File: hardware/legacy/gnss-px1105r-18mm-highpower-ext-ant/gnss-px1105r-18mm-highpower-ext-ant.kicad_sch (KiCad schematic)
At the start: 32 parts, among them J4 BM05B-SRSS-TB, J9 2337019-1, U1 PX1105R, U3 TPS62913RPUR

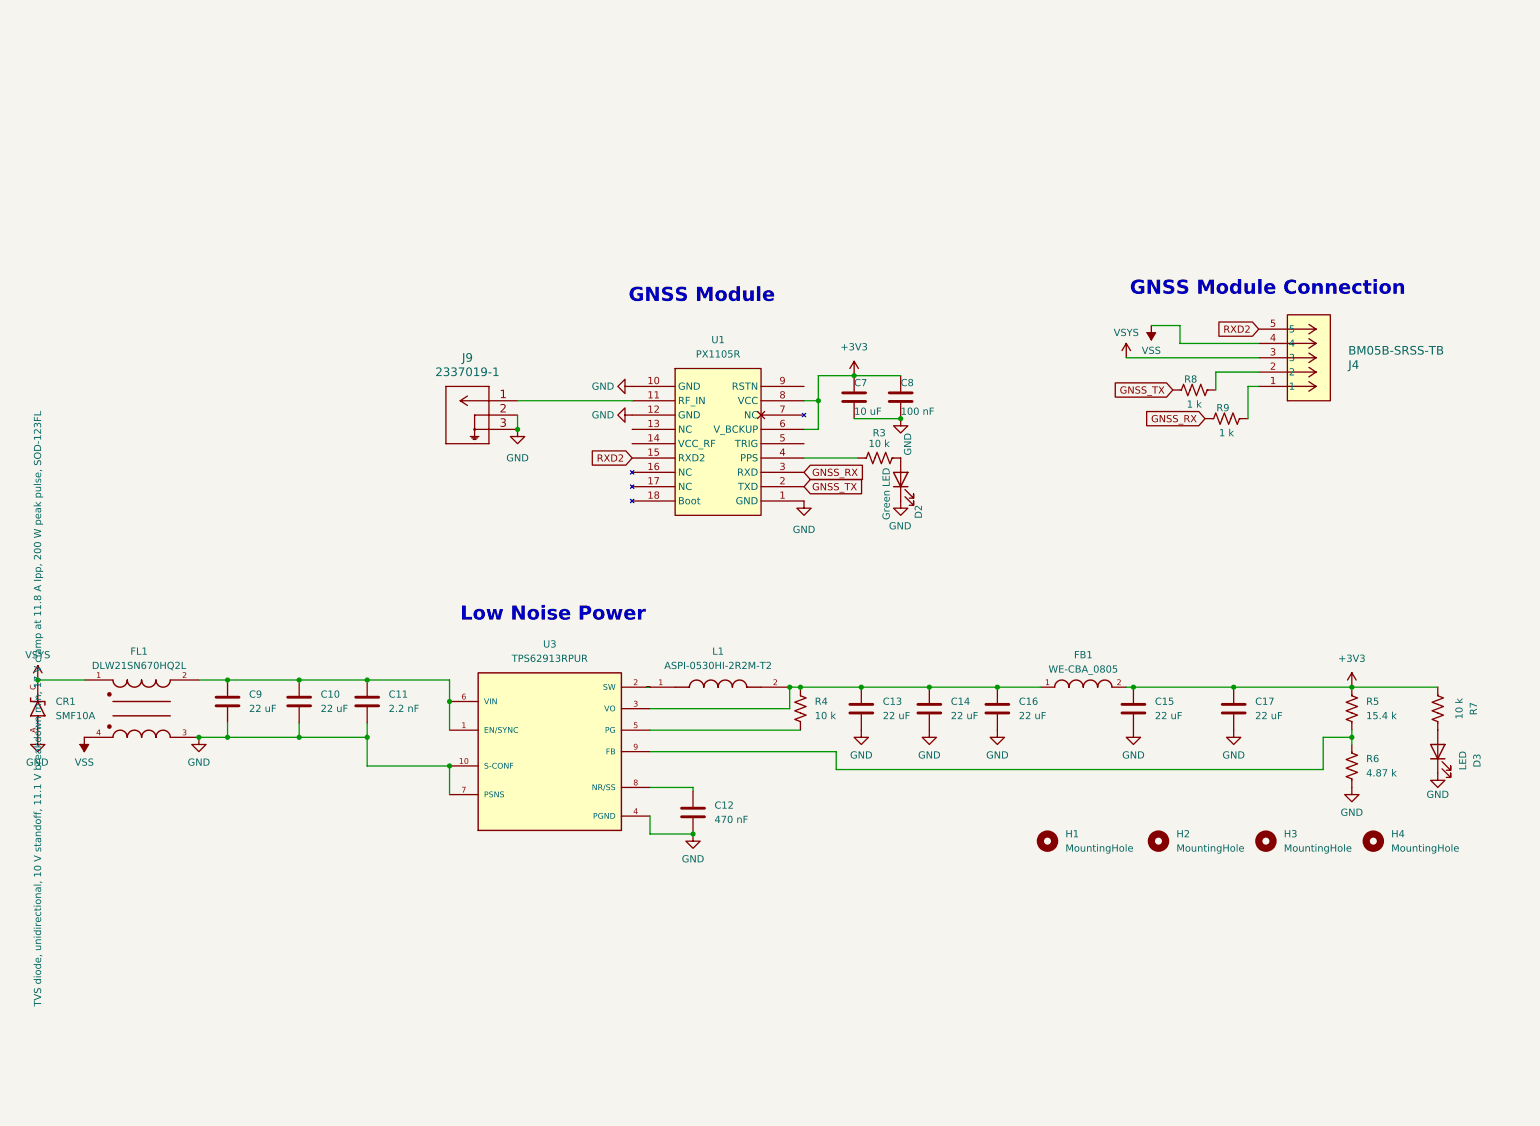
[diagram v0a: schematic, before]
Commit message: hardware(Space Bug): the PX1105R board redrawn as the Space Bug V2 -- ESP32-P4, IMU and a patch-antenna front end on 8 layers, its design review and fixes, and fab notes for the order (#1547)
hardware/legacy/gnss-px1105r-18mm-highpower-ext-ant now holds a new board:
35 x 35 mm, 8 layers on JLC08161H-2116. The PX1105R receiver sits on its own
LDO behind a filter-first dual-band front end (SAW, LNA, SAW, LNA) for a patch
antenna on the back, with an ESP32-P4 (chip revision v3.x) and 16 MB boot
flash, an ISM6HG256X IMU and USB-C. It keeps V2: the 4-layer V2 of 2026-08-15
was never fabricated (docs/board-versioning.md).

The design review (design-review-2026-09-27.md) now opens with a status table.
Fixed here, one finding at a time with the owner:
- Layout: L1 GNSS plane confined west of FL3; L2 feed keep-out on In3-In6;
  L3/L4 return vias; L6 test-pad traces; L7 vias in U2's exposed pad; L8 buck
  input and PGND; L9/L10 P4 supply widths and decoupling; L11 flash ground;
  L12 R11 at J4; L13 three fiducials; L15 different-net vias at 0.25 mm.
- Schematic: S2 J4's tabs to GND; S4 the receiver's BOOT_SEL on GPIO15
  through a DTC123J (Q1). D2 fills the four sheets' title blocks.
- Shared footprints: S8 PX1105R pasted at full pad; S9 QFN-16 keeps only its
  four panes; S10 TSNP single mask window and DPY +0.05 mm mask; S11 the
  SOIC-8-EP paste becomes four 1.0 mm panes. The SAM carrier's U2 shows a
  library mismatch until it is updated from the library.
- S7: cables.md says what a reversed 5-pin cable does to this board.
- D1/D7: FABRICATION-NOTES.md carries the block for the order: stackup,
  ENIG, Type VII vias (161 in lands), RF 0.18/0.20 mm = 50 ohm, mask webs,
  minimums, stencil, U1's 240 C reflow ceiling, placement and hand work.
- The board setup declares filled and capped vias, as the other multilayer
  boards do. Gerbers, drills and the job file are byte-identical either way.

Checks: DRC 0 errors, 0 unconnected (10 old silk/library warnings; 8 parity
warnings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
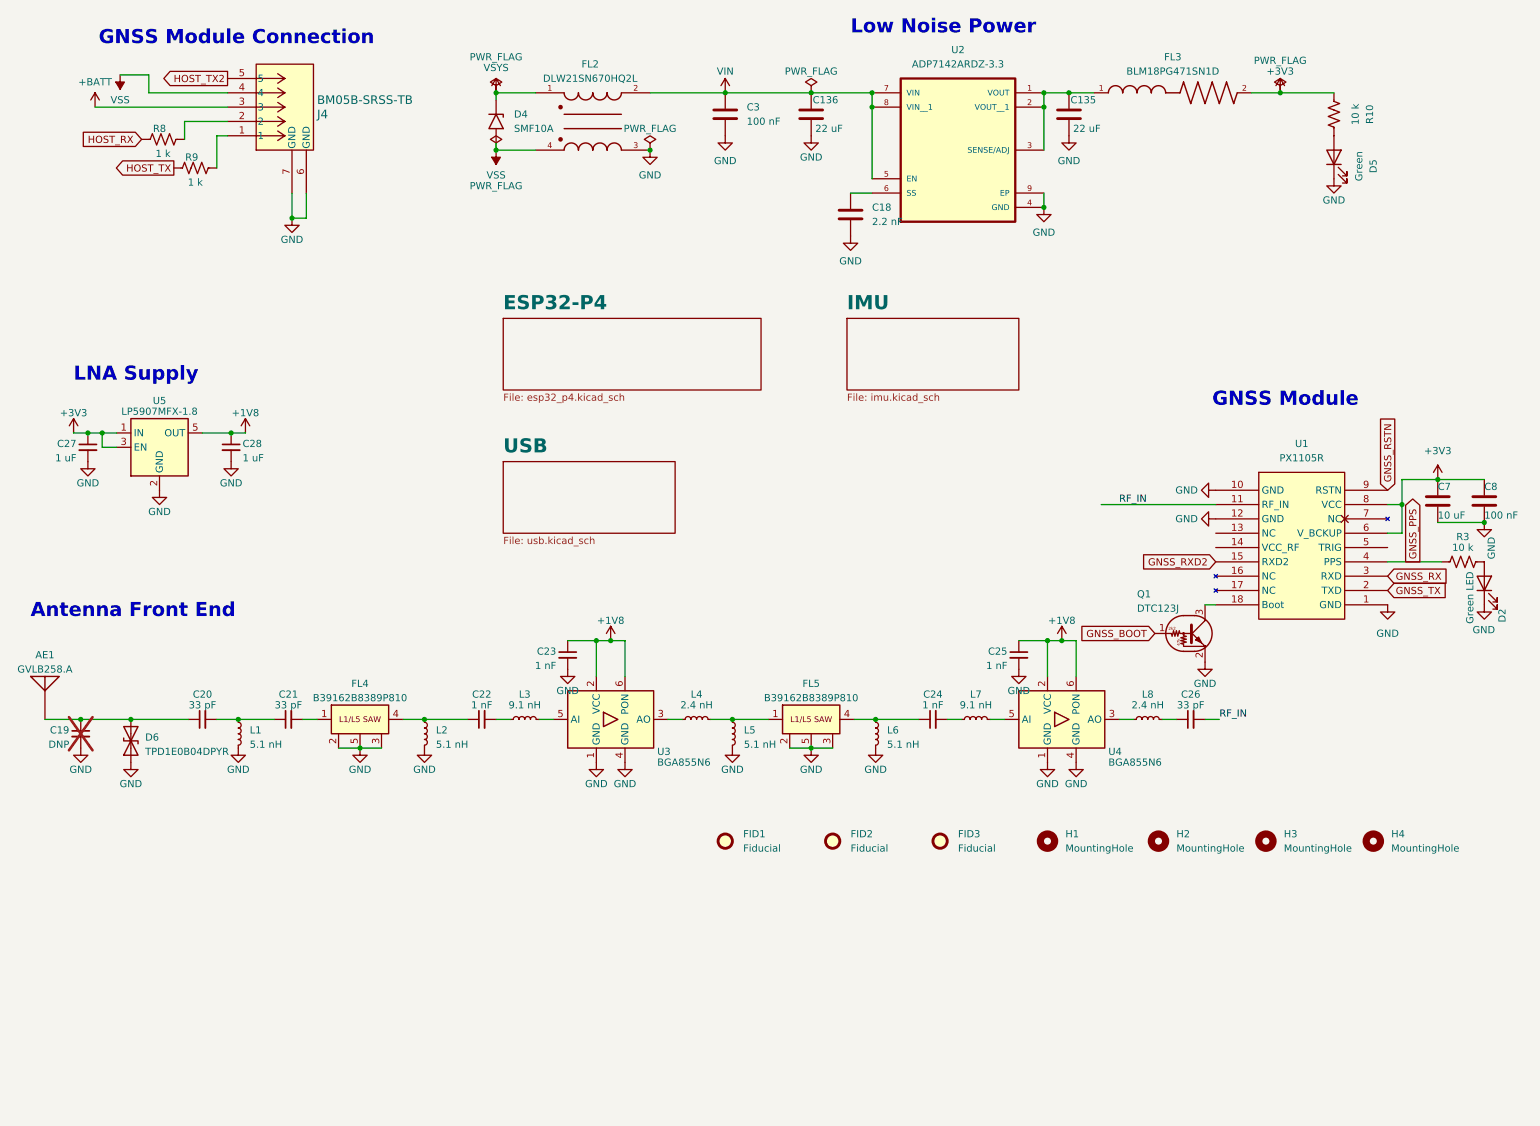
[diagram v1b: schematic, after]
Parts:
- removed C10, C13, C14, C15, C16, C17, C9: 22 uF, Capacitor_SMD:C_0805_2012Metric, symbol Device:C
- removed C11: 2.2 nF, Capacitor_SMD:C_0402_1005Metric, symbol Device:C
- removed C12: 470 nF, Capacitor_SMD:C_0402_1005Metric, symbol Device:C
- removed CR1: SMF10A, Footprints:SODFL3617X108N, symbol Custom:SMF10A
- removed D3: LED, LED_SMD:LED_0402_1005Metric, symbol Device:LED
- removed FB1: WE-CBA_0805, Footprints:WE-CBA_0805_W4.0, symbol Custom:WE-CBA_0805
- removed FL1: DLW21SN670HQ2L, Footprints:FIL_DLW21SN670HQ2L, symbol Custom:DLW21SN670HQ2L
- removed J9: 2337019-1, Footprints:2337019-1, symbol Custom Library:2337019-1
- removed L1: ASPI-0530HI-2R2M-T2, Footprints:IND_ASPI-0530HI-2R2M-T2, symbol Custom:ASPI-0530HI-2R2M-T2
- removed R4, R7: 10 k, Resistor_SMD:R_0402_1005Metric, symbol Device:R_US
- removed R5: 15.4 k, Resistor_SMD:R_0402_1005Metric, symbol Device:R_US
- removed R6: 4.87 k, Resistor_SMD:R_0402_1005Metric, symbol Device:R_US
- removed U3: TPS62913RPUR, Footprints:IC_TPS62913RPUR, symbol Custom:TPS62913RPUR
- added AE1: GVLB258.A, Footprints:ANT_GVLB258.A_TAOGLAS, symbol Custom:GVLB258.A
- added C135, C136: 22 uF, Capacitor_SMD:C_0805_2012Metric, symbol Device:C
- added C18: 2.2 nF, Capacitor_SMD:C_0402_1005Metric, symbol Device:C
- added C19: DNP, Capacitor_SMD:C_0402_1005Metric, symbol Device:C_Small
- added C20, C21, C26: 33 pF, Capacitor_SMD:C_0402_1005Metric, symbol Device:C_Small
- added C22, C23, C24, C25: 1 nF, Capacitor_SMD:C_0402_1005Metric, symbol Device:C_Small
- added C27, C28: 1 uF, Capacitor_SMD:C_0402_1005Metric, symbol Device:C_Small
- added C3: 100 nF, Capacitor_SMD:C_0402_1005Metric, symbol Device:C
- added D4: SMF10A, Diode_SMD:D_SMF, symbol Diode:SMF10A
- added D5: Green, LED_SMD:LED_0402_1005Metric, symbol Device:LED
- added D6: TPD1E0B04DPYR, Footprints:Texas_DPY0002A_0.6x1mm_P0.65mm, symbol Device:D_TVS
- added FID1, FID2, FID3: Fiducial, Fiducial:Fiducial_0.5mm_Mask1mm, symbol Mechanical:Fiducial
- added FL2: DLW21SN670HQ2L, Footprints:FIL_DLW21SN670HQ2L, symbol Custom:DLW21SN670HQ2L
- added FL3: BLM18PG471SN1D, Footprints:BEADC1608X95N, symbol Custom:BLM18PG471SN1D
- added FL4, FL5: B39162B8389P810, Footprints:FIL_SAW-5_1.4x1.1mm_RF360, symbol Custom:B39162B8389P810
- added L1, L2, L5, L6: 5.1 nH, Inductor_SMD:L_0402_1005Metric, symbol Device:L_Small
- added L3, L7: 9.1 nH, Inductor_SMD:L_0402_1005Metric, symbol Device:L_Small
- added L4, L8: 2.4 nH, Inductor_SMD:L_0402_1005Metric, symbol Device:L_Small
- added Q1: DTC123J, Footprints:TRANS_SOT-416_EMT3-EMT3F_ROHM, symbol Transistor_BJT:DTC123J
- added R10: 10 k, Resistor_SMD:R_0402_1005Metric, symbol Device:R_US
- added U2: ADP7142ARDZ-3.3, Footprints:SOIC127P600X175-9N, symbol Custom:ADP7142ARDZ
- added U3, U4: BGA855N6, Footprints:Infineon_PG-TSNP-6-10_0.7x1.1mm_P0.4mm, symbol Custom:BGA855N6
- added U5: LP5907MFX-1.8, Package_TO_SOT_SMD:SOT-23-5, symbol Regulator_Linear:LP5907MFX-1.8
- C7: MPN (none) -> CL21A106KOQNNNE; Mfr (none) -> Samsung
- C8: MPN (none) -> CL05B104KO5NNNC; Mfr (none) -> Samsung
- D2: MPN (none) -> XL-1005UGC; Mfr (none) -> Xinglight
- J4: MPN (none) -> BM05B-SRSS-TB; Mfr (none) -> JST
- R3: MPN (none) -> RC0402FR-0710KL; Mfr (none) -> Yageo
- R8, R9: MPN (none) -> RC0402FR-071KL; Mfr (none) -> Yageo
- U1: MPN (none) -> PX1105R; Mfr (none) -> SkyTraq
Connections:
- net +3V3: now also C27.1, FL3.2, R10.1, U5.1 (IN), U5.3 (EN)
- net GND: now also J4.6 (GND), J4.7 (GND), C135.2, C136.2, C18.2, C19.2, C23.2, C25.2, C27.2, C28.2, C3.2, D5.1 (K), D6.1 (A1), FL2.3, FL4.2 (GND), FL4.3 (GND), FL4.5 (GND), FL5.2 (GND), FL5.3 (GND), FL5.5 (GND), L1.2, L2.2, L5.2, L6.2, Q1.2 (E), U2.4 (GND), U2.9 (EP), U3.1 (GND), U3.4 (GND), U4.1 (GND), U4.4 (GND), U5.2 (GND)
- net GNSS_RX: no longer R9.1
- net GNSS_TX: no longer R8.1
- net VSS: now also D4.2 (A2), FL2.4
- net VSYS: now also D4.1 (A1), FL2.1; no longer J4.3
- net GNSS_PPS: now reaches R3.1, U1.4 (PPS)
- net RF_IN: now reaches U1.11 (RF_IN)
- net RF_IN: now also C26.2
- net at U1.18 (Boot): now also Q1.3 (C)
- net GNSS_RSTN: now reaches U1.9 (RSTN)
- net RXD2 renamed GNSS_RXD2
- net GNSS_RXD2: no longer J4.5
- new net: C22.2, L3.1
- new net: L3.2, U3.5 (AI)
- new net: C22.1, FL4.4 (OUT), L2.1
- new net: L4.1, U3.3 (AO)
- new net: FL5.1 (IN), L4.2, L5.1
- new net: C20.2, C21.1, L1.1
- new net: C26.1, L8.2
- new net: C24.1, FL5.4 (OUT), L6.1
- new net: C24.2, L7.1
- new net: C18.1, U2.6 (SS)
- new net: D5.2 (A), R10.2
- new net: L7.2, U4.5 (AI)
- new net: C135.1, FL3.1, U2.1 (VOUT), U2.2 (VOUT__1), U2.3 (SENSE/ADJ)
- new net: L8.1, U4.3 (AO)
- new net: C21.2, FL4.1 (IN)
- new net: AE1.1 (FEED), C19.1, C20.1, D6.2 (A2)
- new net +1V8: C23.1, C25.1, C28.1, U3.2 (VCC), U3.6 (PON), U4.2 (VCC), U4.6 (PON), U5.5 (OUT)
- new net +BATT: J4.3
- new net GNSS_BOOT: Q1.1 (B)
- new net HOST_RX: R8.1
- new net HOST_TX: R9.1
- new net HOST_TX2: J4.5
- new net VIN: C136.1, C3.1, FL2.2, U2.5 (EN), U2.7 (VIN), U2.8 (VIN__1)
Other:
- added sheet ESP32-P4 (esp32_p4.kicad_sch)
- added sheet IMU (imu.kicad_sch)
- added sheet USB (usb.kicad_sch)
- note added: "Antenna Front End"
- note added: "LNA Supply"
- company: (none) -> TinkerRocket
- title: (none) -> Space Bug
- moved on the sheet: C7, C8, D2, R3, R8, R9

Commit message: hardware: the 1 uF 0402 caps consolidate on the 16 V CL05A105KO5NNNC, with the pending part and layout work
Every GRM155R61A105KE15D (Murata, 10 V X5R) becomes the Samsung CL05A105KO5NNNC (16 V X5R) on
space-bug-m8t, gnss-sdr-dev and the legacy gnss-px1105r board -- 34 symbols and their 34 footprints.
Same 0402 footprint, so only the MPN and Mfr change. The higher-rated part is already the 1 uF used
on the Tinker boards, so the BOMs now carry one 1 uF line instead of two.

Pending work committed alongside:
- space-bug-m8t: the 10 uF bulk caps go to CL21A226MOQNNNE, added CL05A106MQ5NUNC, RC0402FR-071KL and
  R-667995 parts, schematic, layout and DRC rule updates, and the new FABRICATION-NOTES.md
- gnss-sdr-dev: the 5.1 nH inductors go from LQG15HS5N1S02D to LQW15AN5N1C00D, added 1 k and 100 k
  resistors, and schematic and layout updates
- legacy gnss-px1105r: the 10 uF caps go to CL21A226MOQNNNE, plus schematic and layout updates
- tinker-beetle: the 390 pF caps go to GRM1555C1H391JA01D, the 100 k resistors to RC0402FR-07100KL,
  and the 2.2 uH inductor from XGL4020-222ME to SRP4020FA-2R2M
- gnss-sam10m8-18mm-hv: the 100 pF cap goes from CL05C101JB5NNNC to GRM1555C1H101JA01D
- the Taoglas CGGBP.25.4.A.02 antenna footprint, and project-file housekeeping

Co-Authored-By: Claude Opus 5.5 <noreply@anthropic.com>
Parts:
- C27, C28: MPN GRM155R61A105KE15D -> CL05A105KO5NNNC; Mfr Murata -> Samsung
- C7: value 10 uF -> 22 uF; MPN CL21A106KOQNNNE -> CL21A226MOQNNNE
